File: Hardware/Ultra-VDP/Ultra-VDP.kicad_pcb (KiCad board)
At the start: 4 copper layers, 60.9 x 26.8 mm, 70 parts, among them J1 BC075-05, J2 BC075-10, J3 CBUS, J4 BC075-10, J5 BC075-06, J6 BC075-10, J7 BC075-10, J8 BC075-05, U14 V53C8125HT30, U3 V9958, U6 LMH1980, Y1 21.477270MHz, Y3 4.433618MHz

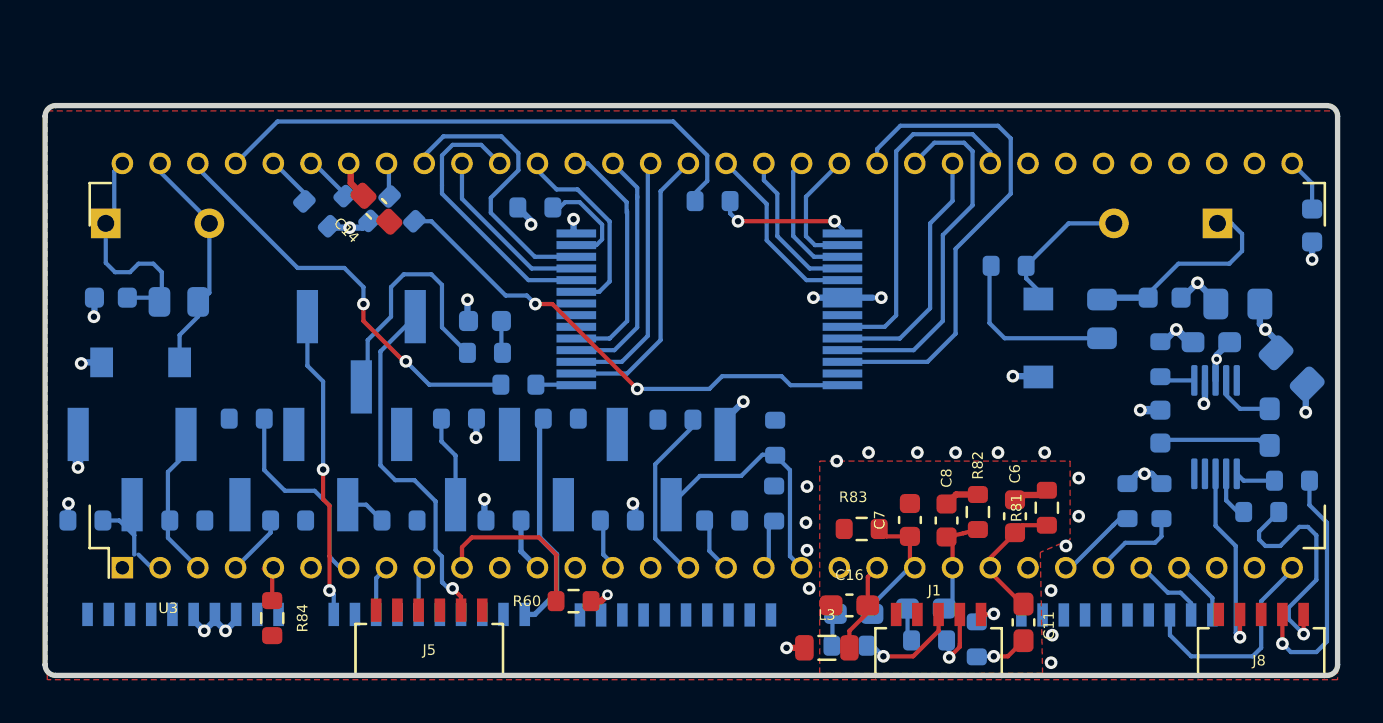
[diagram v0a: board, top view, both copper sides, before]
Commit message: Finished the VDP-board, finished up the mixer-section, removed the buffer-pins from the FPGA, and instead added external buffers for the slots, designed a marquee-block with the Ultra-MSX logo, designed the logotype, andmultiple other changes.
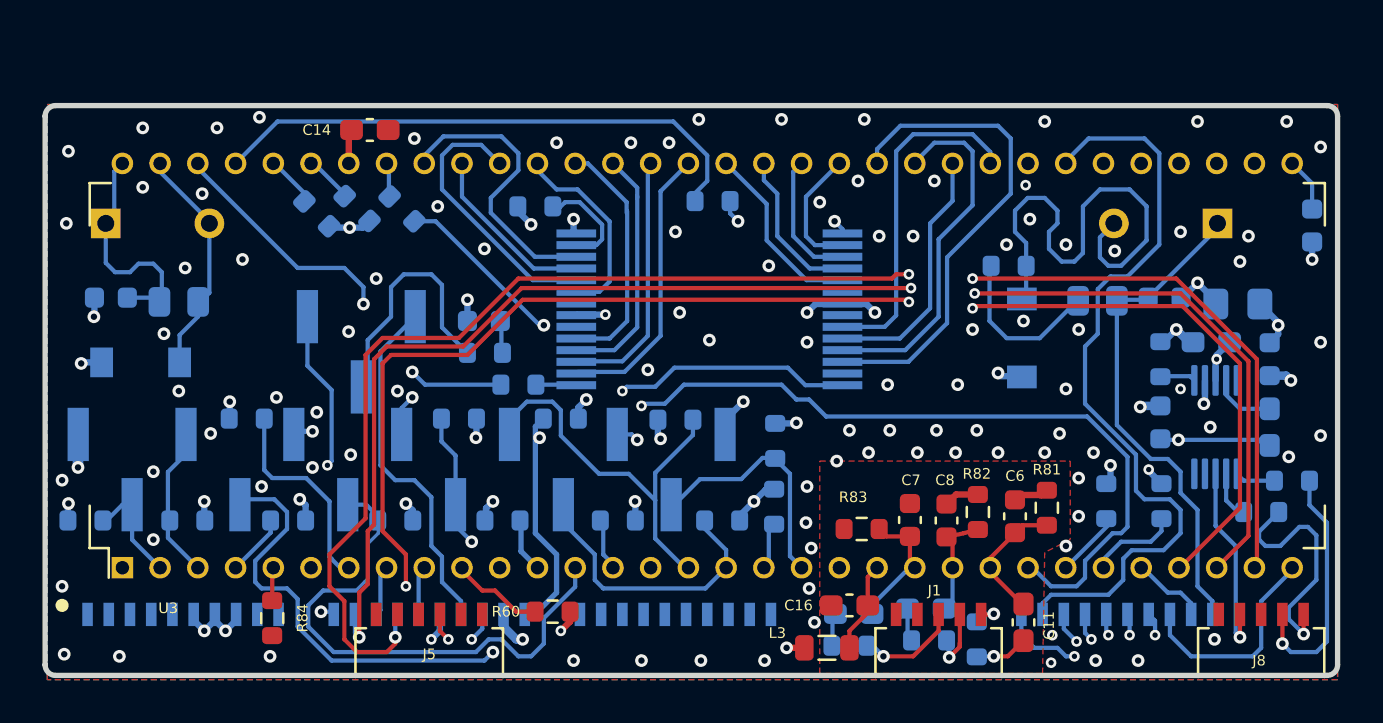
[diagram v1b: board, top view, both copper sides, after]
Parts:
- removed C89: C_GRM21BR71A106KA73K, Capacitor_SMD:C_0805_2012Metric_Pad1.18x1.45mm_HandSolder
- added C18: C_GRM188D71A106KA73D, Capacitor_SMD:C_0603_1608Metric, B.Cu at (152.8, 102.4)
- moved C14 3.72 mm to (110.4, 91.6), turned to 180 degrees
- moved R60 1.10 mm to (119.0, 114.3)
- moved R21 1.00 mm to (145.1, 109.1)
- moved R4 0.88 mm to (144.7, 99.7), turned to 0 degrees
- moved C5 0.78 mm to (141.1, 101.4)
- moved C12 0.20 mm to (147.7, 105.4)
- moved J5 0.20 mm to (113.2, 115.2)
- moved R53 0.20 mm to (111.6, 110.0)
- moved R23 0.15 mm to (129.5, 106.2)
- moved R25 0.15 mm to (129.4, 109.3)
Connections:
- J4 pad 4: GND -> /PAL_CLK_OUT
- J5 pad 3: /PAL_CLK_IN+ -> GND
- J5 pad 4: GND -> /A0
- J5 pad 5: /PAL_CLK_OUT -> GND
- J6 pad 1: /A0 -> /PAL_CLK_IN+
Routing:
- net /~{VDP_RD}: track 0.00 -> 73.7 mm, vias 0 -> 3
- net /~{VDP_WR}: track 0.00 -> 68.9 mm, vias 0 -> 3
- net /A0: track 2.97 -> 69.6 mm, vias 0 -> 4
- net /~{VDP_WAIT}: track 3.94 -> 58.4 mm, vias 0 -> 1
- net /COMPSYNC: track 5.30 -> 54.1 mm, vias 0 -> 1
- net /~{VDP_INT}: track 10.5 -> 50.8 mm, vias 0 -> 2
- net /D0: track 0.00 -> 39.7 mm, vias 0 -> 1
- net /D1: track 0.00 -> 36.6 mm
- net /D3: track 0.00 -> 34.3 mm, vias 0 -> 1
- net /D2: track 0.00 -> 33.4 mm, vias 0 -> 1
- net /D6: track 0.00 -> 31.2 mm, vias 0 -> 1
- net /D5: track 0.00 -> 30.9 mm, vias 0 -> 1
- net /D4: track 0.00 -> 29.7 mm, vias 0 -> 1
- net /CBDR: track 0.00 -> 24.3 mm, vias 0 -> 1
- net /CB6: track 1.92 -> 25.7 mm
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- added copper zone on B.Cu, net GND
- added copper zone on In1.Cu, net GND

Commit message: Redesigned VDP-board to include a socket, increased it to 4 layers. Various clean-ups here and there. Improved the printer-port and joystick-port 3D-models. Improved the cooling-fin 3D-model, and added attachment-spring in 3D-model.
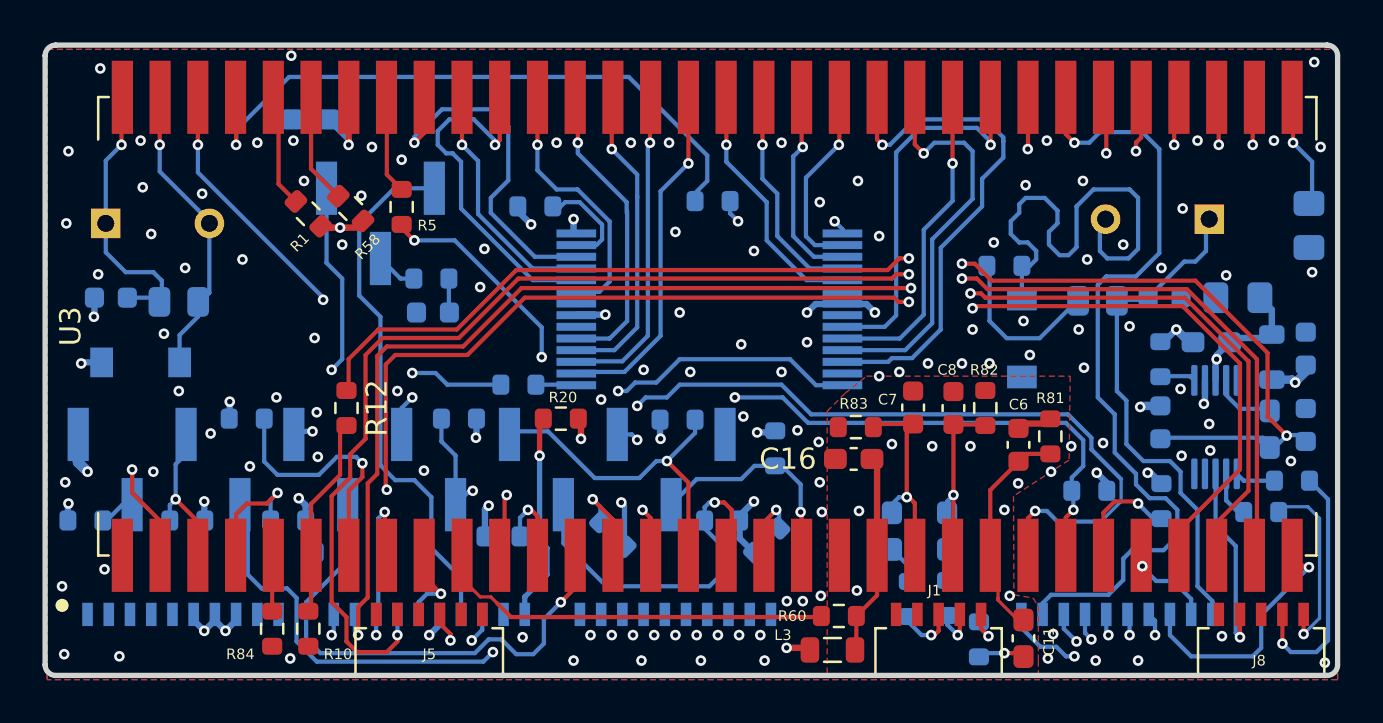
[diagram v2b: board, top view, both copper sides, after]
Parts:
- added C19: 47pF, Capacitor_SMD:C_0603_1608Metric, B.Cu at (154.5, 105.5)
- added L1: L_MLZ2012M4R7HT000, Inductor_SMD:L_0805_2012Metric, B.Cu at (152.9, 102.3)
- added R10: 75, Resistor_SMD:R_0603_1608Metric, F.Cu at (107.5, 115.1)
- added R12: 100, Resistor_SMD:R_0603_1608Metric, F.Cu at (109.3, 104.7)
- C14: moved to B.Cu
- C3: value 0.1uF -> C_CL21B223KBANFNC; footprint Capacitor_SMD:C_0603_1608Metric -> Capacitor_SMD:C_0805_2012Metric_Pad1.18x1.45mm_HandSolder
- R1, R20, R5, R58: moved to F.Cu
- U3: footprint Ultra-MSX:IC_SDIP64_600 -> Ultra-MSX:DIP-64_W19.05mm_SMDSocket_SmallPads
- moved R60 13.5 mm to (132.5, 114.5)
- moved C16 6.90 mm to (133.2, 107.1)
- moved JP5 6.12 mm to (110.9, 96.0)
- moved C8 5.31 mm to (137.9, 104.7)
- moved C7 5.30 mm to (136.0, 104.7)
- moved R82 4.91 mm to (139.4, 104.7)
- moved R83 4.81 mm to (133.3, 105.6)
- moved R11 4.32 mm to (113.3, 98.6)
- moved C10 4.30 mm to (135.0, 110.5), turned to 90 degrees
- moved C9 3.78 mm to (137.6, 110.5), turned to 90 degrees
- moved R14 3.56 mm to (135.8, 113.7), turned to 90 degrees
- moved R81 3.37 mm to (142.5, 106.0)
- moved C6 3.37 mm to (141.0, 106.4)
- moved R53 3.31 mm to (108.7, 111.5), turned to 180 degrees
- moved C14 2.84 mm to (107.6, 91.1), turned to 0 degrees
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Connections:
- net /PALCLK_JPR renamed /NTSC_CLKO
- net Net-(R84-Pad1) renamed /HORSYNC
- C12 pad 1: /COMPSYNC -> Net-(C12-Pad1)
- C15 pad 2: /COMPSYNC -> Net-(C12-Pad1)
- C17 pad 1: +5V -> /+5V_SYNC
- C3 pad 1: GND -> Net-(C3-Pad1)
- C3 pad 2: Net-(C3-Pad2) -> GND
- C73 pad 1: +5V -> /+5V_SYNC
- R20 pad 1: /~{VDP_INT} -> +5V
- R20 pad 2: +5V -> /~{VDP_INT}
- R60 pad 2: +5V -> VCCVDP
- U3 pad 33: Net-(C3-Pad2) -> Net-(C3-Pad1)
- U6 pad 3: +5V -> /+5V_SYNC
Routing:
- net Net-(C12-Pad1): track 0.00 -> 60.3 mm, vias 0 -> 3
- net /COMPSYNC: track 54.1 -> 10.3 mm, vias 1 -> 0
- net /~{YS}: track 4.37 -> 18.8 mm
- net /~{VDP_WAIT}: track 58.4 -> 47.0 mm, vias 1 -> 3
- net GND: track 25.6 -> 15.5 mm
- net Net-(JP5-Pad2): track 11.8 -> 1.97 mm
- net /PAL_CLK_OUT: track 16.8 -> 25.2 mm
- net /NTSC_CLKO: track 16.4 -> 24.2 mm
- net VCCVDP: track 4.31 -> 10.9 mm
- net /+5V_SYNC: track 0.00 -> 6.18 mm, vias 0 -> 1
- net Net-(C3-Pad1): track 0.00 -> 5.65 mm, vias 0 -> 1
- net /CLK_VDP: track 2.40 -> 8.04 mm, vias 0 -> 2
- net /CBDR: track 24.3 -> 28.7 mm, vias 1 -> 2
- net /D4: track 29.7 -> 34.0 mm, vias 1 -> 2
- net /CB2: track 13.6 -> 17.8 mm, vias 0 -> 1
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- added copper zone on In1.Cu, net GNDA
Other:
- board size 60.9 x 26.8 mm -> 60.9 x 29.7 mm

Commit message: Generated first PDF-files
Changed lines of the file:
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@@
     (thickness 2)
   )
-  (paper "A4")
+  (paper "A3")
+  (title_block
+    (date "2022-07-20")
+  )
   (layers
     (0 "F.Cu" signal)
@@
     (grid_origin 95.1 117.3)
     (pcbplotparams
-      (layerselection 0x00010fc_ffffffff)
+      (layerselection 0x00310fc_ffffffff)
       (disableapertmacros false)
       (usegerberextensions false)
@@
       (svgprecision 6)
       (excludeedgelayer true)
-      (plotframeref false)
+      (plotframeref true)
       (viasonmask false)
       (mode 1)
@@
       (psa4output false)
       (plotreference true)
-      (plotvalue true)
+      (plotvalue false)
       (plotinvisibletext false)
       (sketchpadsonfab false)
       (subtractmaskfromsilk false)
-      (outputformat 1)
+      (outputformat 4)
       (mirror false)
-      (drillshape 1)
+      (drillshape 0)
       (scaleselection 1)
       (outputdirectory "")
@@
     (fp_line (start 1 0.625) (end 1 -0.625) (layer "B.Fab") (width 0.1))
     (fp_line (start 1 -0.625) (end -1 -0.625) (layer "B.Fab") (width 0.1))
-    (pad "1" smd roundrect (at -0.9125 0) (size 1.025 1.4) (layers "B.Cu" "B.Paste" "B.Mask") (roundrect_rratio 0.243902)
+    (pad "1" smd roundrect (at -0.9125 0) (size 1.025 1.4) (layers "B.Cu" "B.Paste" "B.Mask") (roundrect_rratio 0.243902439)
       (net 34 "Net-(R3-Pad2)") (pintype "passive"))
-    (pad "2" smd roundrect (at 0.9125 0) (size 1.025 1.4) (layers "B.Cu" "B.Paste" "B.Mask") (roundrect_rratio 0.243902)
+    (pad "2" smd roundrect (at 0.9125 0) (size 1.025 1.4) (layers "B.Cu" "B.Paste" "B.Mask") (roundrect_rratio 0.243902439)
       (net 114 "/PAL_CLK_IN+") (pintype "passive"))
     (model "${KICAD6_3DMODEL_DIR}/Resistor_SMD.3dshapes/R_0805_2012Metric.wrl"
@@
     (fp_line (start -1 0.625) (end 1 0.625) (layer "B.Fab") (width 0.1))
     (fp_line (start -1 -0.625) (end -1 0.625) (layer "B.Fab") (width 0.1))
-    (pad "1" smd roundrect (at -1.0375 0 270) (size 1.175 1.45) (layers "B.Cu" "B.Paste" "B.Mask") (roundrect_rratio 0.212766)
+    (pad "1" smd roundrect (at -1.0375 0 270) (size 1.175 1.45) (layers "B.Cu" "B.Paste" "B.Mask") (roundrect_rratio 0.2127659574)
       (net 31 "Net-(C3-Pad1)") (pinfunction "1") (pintype "passive"))
-    (pad "2" smd roundrect (at 1.0375 0 270) (size 1.175 1.45) (layers "B.Cu" "B.Paste" "B.Mask") (roundrect_rratio 0.212766)
+    (pad "2" smd roundrect (at 1.0375 0 270) (size 1.175 1.45) (layers "B.Cu" "B.Paste" "B.Mask") (roundrect_rratio 0.2127659574)
       (net 1 "GND") (pinfunction "2") (pintype "passive"))
     (model "${KICAD6_3DMODEL_DIR}/Capacitor_SMD.3dshapes/C_0805_2012Metric.wrl"
@@
     (fp_line (start 1 -0.625) (end -1 -0.625) (layer "B.Fab") (width 0.1))
     (fp_line (start 1 0.625) (end 1 -0.625) (layer "B.Fab") (width 0.1))
-    (pad "1" smd roundrect (at -0.9125 0) (size 1.025 1.4) (layers "B.Cu" "B.Paste" "B.Mask") (roundrect_rratio 0.243902)
+    (pad "1" smd roundrect (at -0.9125 0) (size 1.025 1.4) (layers "B.Cu" "B.Paste" "B.Mask") (roundrect_rratio 0.243902439)
       (net 113 "/XTAL-") (pintype "passive"))
-    (pad "2" smd roundrect (at 0.9125 0) (size 1.025 1.4) (layers "B.Cu" "B.Paste" "B.Mask") (roundrect_rratio 0.243902)
+    (pad "2" smd roundrect (at 0.9125 0) (size 1.025 1.4) (layers "B.Cu" "B.Paste" "B.Mask") (roundrect_rratio 0.243902439)
       (net 2 "/XTAL1+") (pintype "passive"))
     (model "${KICAD6_3DMODEL_DIR}/Resistor_SMD.3dshapes/R_0805_2012Metric.wrl"
@@
     (fp_line (start -1 -0.625) (end -1 0.625) (layer "B.Fab") (width 0.1))
     (fp_line (start 1 0.625) (end 1 -0.625) (layer "B.Fab") (width 0.1))
-    (pad "1" smd roundrect (at -1.0375 0 180) (size 1.175 1.45) (layers "B.Cu" "B.Paste" "B.Mask") (roundrect_rratio 0.212766)
+    (pad "1" smd roundrect (at -1.0375 0 180) (size 1.175 1.45) (layers "B.Cu" "B.Paste" "B.Mask") (roundrect_rratio 0.2127659574)
       (net 115 "/+5V_SYNC") (pinfunction "1") (pintype "passive"))
-    (pad "2" smd roundrect (at 1.0375 0 180) (size 1.175 1.45) (layers "B.Cu" "B.Paste" "B.Mask") (roundrect_rratio 0.212766)
+    (pad "2" smd roundrect (at 1.0375 0 180) (size 1.175 1.45) (layers "B.Cu" "B.Paste" "B.Mask") (roundrect_rratio 0.2127659574)
       (net 1 "GND") (pinfunction "2") (pintype "passive"))
     (model "${KICAD6_3DMODEL_DIR}/Capacitor_SMD.3dshapes/C_0805_2012Metric.wrl"
